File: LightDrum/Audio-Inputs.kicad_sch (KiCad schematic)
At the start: 52 parts, among them J201 XLR3, J202 SJ-43515RS-SMT-TR, Q201 NX6008NBKWX, Q202 NX6008NBKWX, U201 MCP3561R, U202 AZV321, U203 MCP3561R, U204 AZV321, U205 AP311A, U206 OPA1652

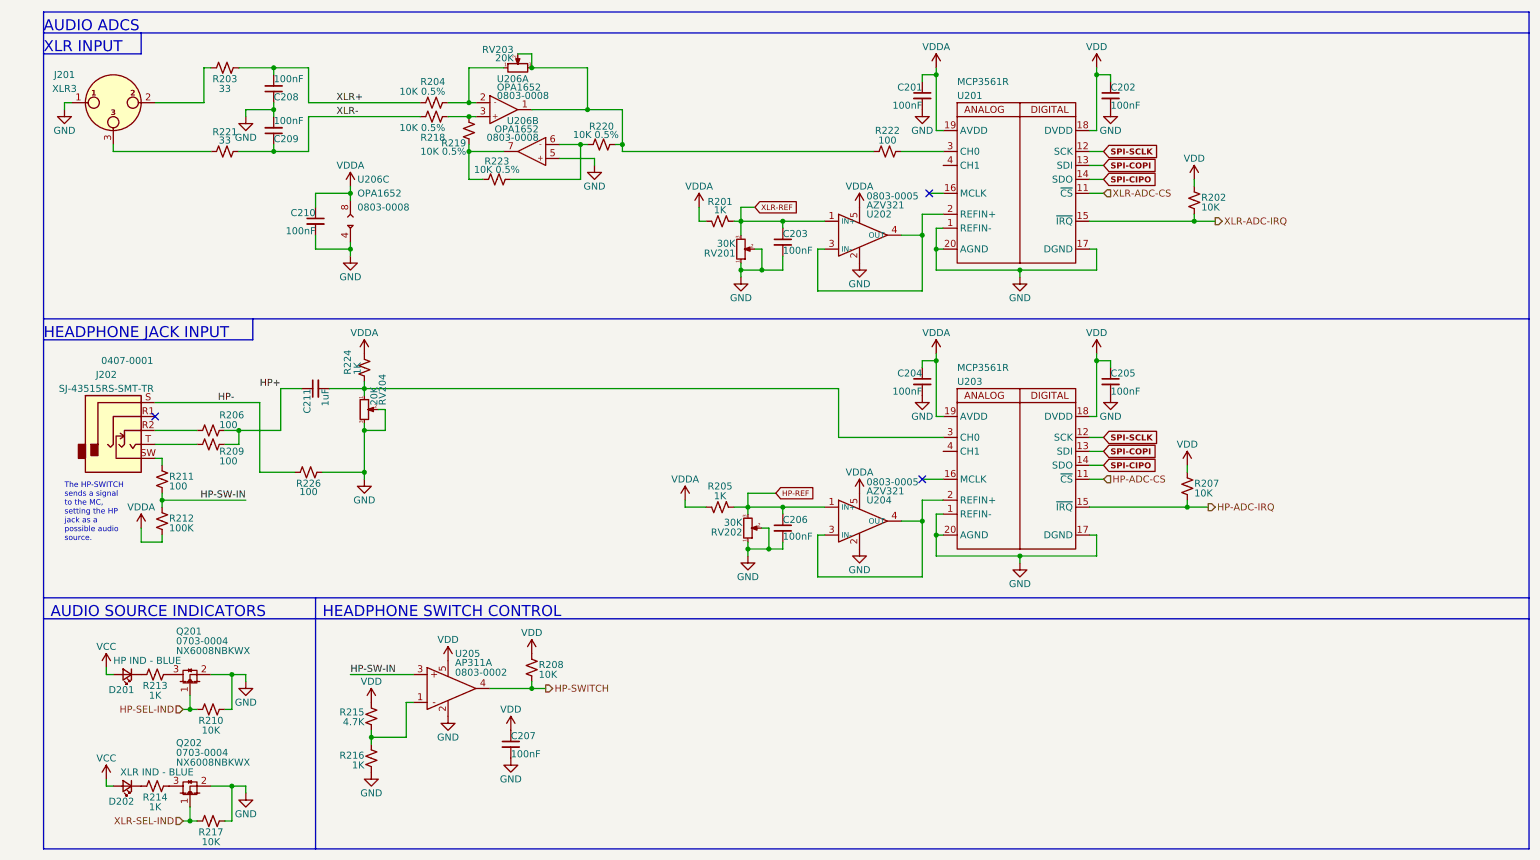
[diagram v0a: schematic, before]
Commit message: Preliminary schematic lock - Starting PCB layout
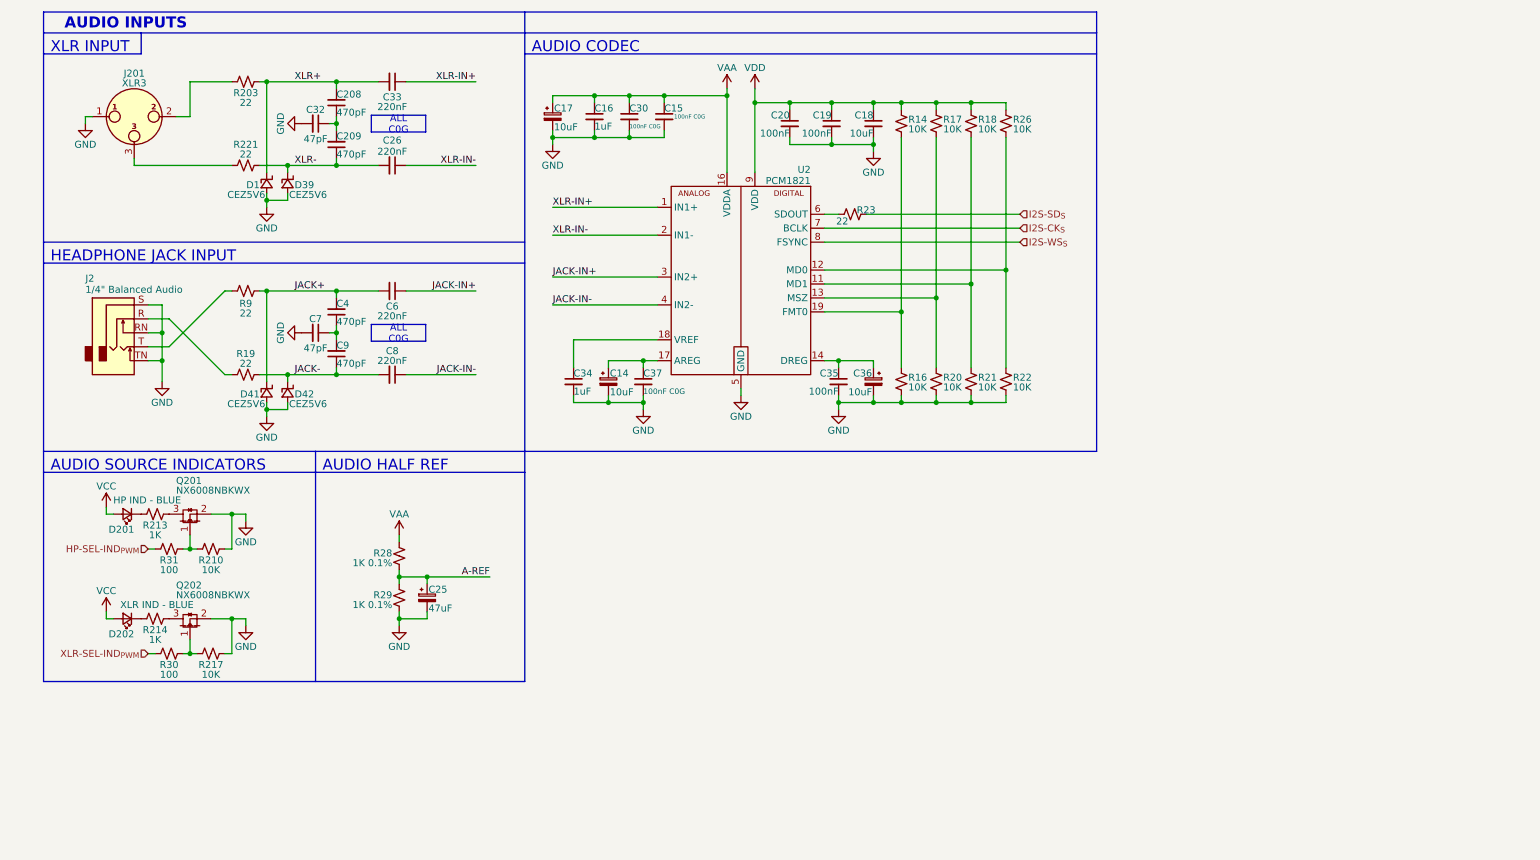
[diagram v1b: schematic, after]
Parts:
- removed C201, C202, C203, C204, C205, C206, C207, C210: 100nF, Capacitor_SMD:C_0603_1608Metric, symbol Device:C_Small
- removed C211: 1uF, Capacitor_SMD:C_0805_2012Metric, symbol Device:C_Small
- removed J201: XLR3, Daxxn_Connectors:CP30082-XLR, symbol Connector:XLR3
- removed J202: SJ-43515RS-SMT-TR, Daxxn_Connectors:SJ-43515RS-SMT-TR, symbol Daxxn_Connectors:SJ-43515RS-SMT-TR
- removed R201, R205: 1K, Resistor_SMD:R_0603_1608Metric, symbol Device:R_Small_US
- removed R202, R207: 10K, Resistor_SMD:R_0603_1608Metric, symbol Device:R_Small_US
- removed R204, R218, R219, R220, R223: 10K 0.5%, Resistor_SMD:R_0603_1608Metric, symbol Device:R_Small_US
- removed R206, R209, R211, R222: 100, Resistor_SMD:R_0805_2012Metric, symbol Device:R_Small_US
- removed R208: 10K, Resistor_SMD:R_0805_2012Metric, symbol Device:R_Small_US
- removed R212: 100K, Resistor_SMD:R_0805_2012Metric, symbol Device:R_Small_US
- removed R215: 4.7K, Resistor_SMD:R_0805_2012Metric, symbol Device:R_Small_US
- removed R216, R224: 1K, Resistor_SMD:R_0805_2012Metric, symbol Device:R_Small_US
- removed R226: 100, Resistor_SMD:R_0603_1608Metric, symbol Device:R_Small_US
- removed RV201, RV202: 30K, Daxxn_Switches:Bourns_3214W_Vertical, symbol Device:R_Potentiometer_Small
- removed RV203, RV204: 20K, Daxxn_Switches:Bourns_3214W_Vertical, symbol Device:R_Potentiometer_Small
- removed U201, U203: MCP3561R, Daxxn_Packages:QFN-20-1EP_3x3mm_P0.4mm_EP1.65x1.65mm, symbol Daxxn_IC:MCP3561R
- removed U202, U204: AZV321, Package_TO_SOT_SMD:SOT-23-5, symbol Daxxn_OPAMP:AZV321
- removed U205: AP311A, Package_TO_SOT_SMD:SOT-23-5, symbol Daxxn_OPAMP:AP311A
- removed U206: OPA1652, Package_SO:VSSOP-8_3.0x3.0mm_P0.65mm, symbol Daxxn_OPAMP:OPA1652
- added C14, C17, C36: 10uF, Capacitor_SMD:CP_Elec_3x5.4, symbol Daxxn_Device:C_Pol
- added C15, C30, C37: 100nF C0G, Capacitor_SMD:C_1206_3216Metric, symbol Device:C_Small
- added C16, C34: 1uF, Capacitor_SMD:C_0603_1608Metric, symbol Device:C_Small
- added C18: 10uF, Capacitor_SMD:C_1210_3225Metric, symbol Device:C_Small
- added C19, C20, C35: 100nF, Capacitor_SMD:C_0402_1005Metric, symbol Device:C_Small
- added C25: 47uF, Capacitor_SMD:CP_Elec_6.3x7.7, symbol Daxxn_Device:C_Pol
- added C26, C33, C6, C8: 220nF, Capacitor_SMD:C_1206_3216Metric, symbol Device:C_Small
- added C32, C7: 47pF, Capacitor_SMD:C_0402_1005Metric, symbol Device:C_Small
- added C4, C9: 470pF, Capacitor_SMD:C_0402_1005Metric, symbol Device:C_Small
- added D1, D39, D41, D42: CEZ5V6, Daxxn_Diodes:D_SOD-523, symbol Daxxn_Device:D_TVS_U
- added J2: 1/4" Balanced Audio, Daxxn_Connectors:SJ-63073E, symbol Daxxn_Connectors:AudioJack3_SwitchTR
- added J201: XLR3, Daxxn_Connectors:CP30082-XLR, symbol Connector_Audio:XLR3
- added R14, R16, R17, R18, R20, R21, R22, R26: 10K, Resistor_SMD:R_0402_1005Metric, symbol Device:R_Small_US
- added R19, R23, R9: 22, Resistor_SMD:R_0402_1005Metric, symbol Device:R_Small_US
- added R28, R29: 1K 0.1%, Resistor_SMD:R_0402_1005Metric, symbol Device:R_Small_US
- added R30, R31: 100, Resistor_SMD:R_0402_1005Metric, symbol Device:R_Small_US
- added U2: PCM1821, Daxxn_Packages:TI-WQFN-RTE-20-3x3mm-P0.5mm-EP1_1.4mm, symbol Daxxn_Audio:PCM1821
- C208, C209: value 100nF -> 470pF; footprint Capacitor_SMD:C_0603_1608Metric -> Capacitor_SMD:C_0402_1005Metric; SupplierPN (none) -> 1276-1117-1-ND
- D202: SupplierPN (none) -> LTST-S321TBKT
- Q201, Q202: SupplierPN (none) -> 1727-NX6008NBKWXCT-ND
- R203, R221: value 33 -> 22; footprint Resistor_SMD:R_0603_1608Metric -> Resistor_SMD:R_0402_1005Metric; SupplierPN (none) -> 2037-PFR05S-220-FNHCT-ND
- R210, R217: footprint Resistor_SMD:R_0805_2012Metric -> Resistor_SMD:R_0402_1005Metric; SupplierPN (none) -> 311-10KJRCT-ND
- R213, R214: footprint Resistor_SMD:R_0805_2012Metric -> Resistor_SMD:R_0402_1005Metric; SupplierPN (none) -> 311-1.0KJRCT-ND
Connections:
- net VDD: now also C18.1, C19.1, C20.1, R14.1, R17.1, R18.1, R26.1, U2.9 (VDD)
- net XLR+: now also C33.2, D1.1 (K)
- net XLR-: now also C26.2, D39.1 (K)
- net at R221.1: now also J201.3
- net at R203.1: now also J201.2
- net AGND renamed GND
- net GND: now also C14.2, C15.2, C16.2, C17.2, C18.2, C19.2, C20.2, C25.2, C30.2, C32.2, C34.2, C35.2, C36.2, C37.2, C7.2, D1.2 (A), D39.2 (A), D41.2 (A), D42.2 (A), J2.RN, J2.S, J2.TN, J201.1, R16.2, R20.2, R21.2, R22.2, R29.1, U2.10 (GND), U2.15 (GND), U2.20 (GND), U2.21 (GND), U2.5 (GND); no longer C208.1, C209.2
- net HP-SEL-IND: no longer names the net of Q201.1 (G), R210.2
- net HP-SEL-IND: now also R31.1
- net XLR-SEL-IND: no longer names the net of Q202.1 (G), R217.2
- net XLR-SEL-IND: now also R30.1
- new net: R17.2, R20.1, U2.13 (MSZ)
- new net: R18.2, R21.1, U2.11 (MD1)
- new net: R22.1, R26.2, U2.12 (MD0)
- new net: C35.1, C36.1, U2.14 (DREG)
- new net: C14.1, C37.1, U2.17 (AREG)
- new net: C34.1, U2.18 (VREF)
- new net: R14.2, R16.1, U2.19 (FMT0)
- new net: R23.2, U2.6 (SDOUT)
- new net: C4.1, C7.1, C9.2
- new net: J2.R, R19.1
- new net: J2.T, R9.1
- new net: C208.1, C209.2, C32.1
- new net A-REF: C25.1, R28.1, R29.2
- new net HP-SEL-IND_{PWM}: R31.2
- new net I2S-CK_{S}: U2.7 (BCLK)
- new net I2S-SD_{S}: R23.1
- new net I2S-WS_{S}: U2.8 (FSYNC)
- new net JACK+: C4.2, C6.2, D41.1 (K), R9.2
- new net JACK-: C8.2, C9.1, D42.1 (K), R19.2
- new net JACK-IN+: C6.1, U2.3 (IN2+)
- new net JACK-IN-: C8.1, U2.4 (IN2-)
- new net VAA: C15.1, C16.1, C17.1, C30.1, R28.2, U2.16 (VDDA)
- new net XLR-IN+: C33.1, U2.1 (IN1+)
- new net XLR-IN-: C26.1, U2.2 (IN1-)
- new net XLR-SEL-IND_{PWM}: R30.2
- no-connect marks 3 -> 0
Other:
- note added: "AUDIO CODEC"
- note added: "AUDIO HALF REF"
- note added: "AUDIO INPUTS"
- note removed: "AUDIO ADCS"
- note removed: "HEADPHONE SWITCH CONTROL"
- note removed: "The HP-SWITCH sends a signal to the MC, setting the HP jack as a possible audio source."
- moved on the sheet: C208, C209, D201, D202, Q201, Q202, R203, R210, R213, R214, R217, R221

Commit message: Component placement complete
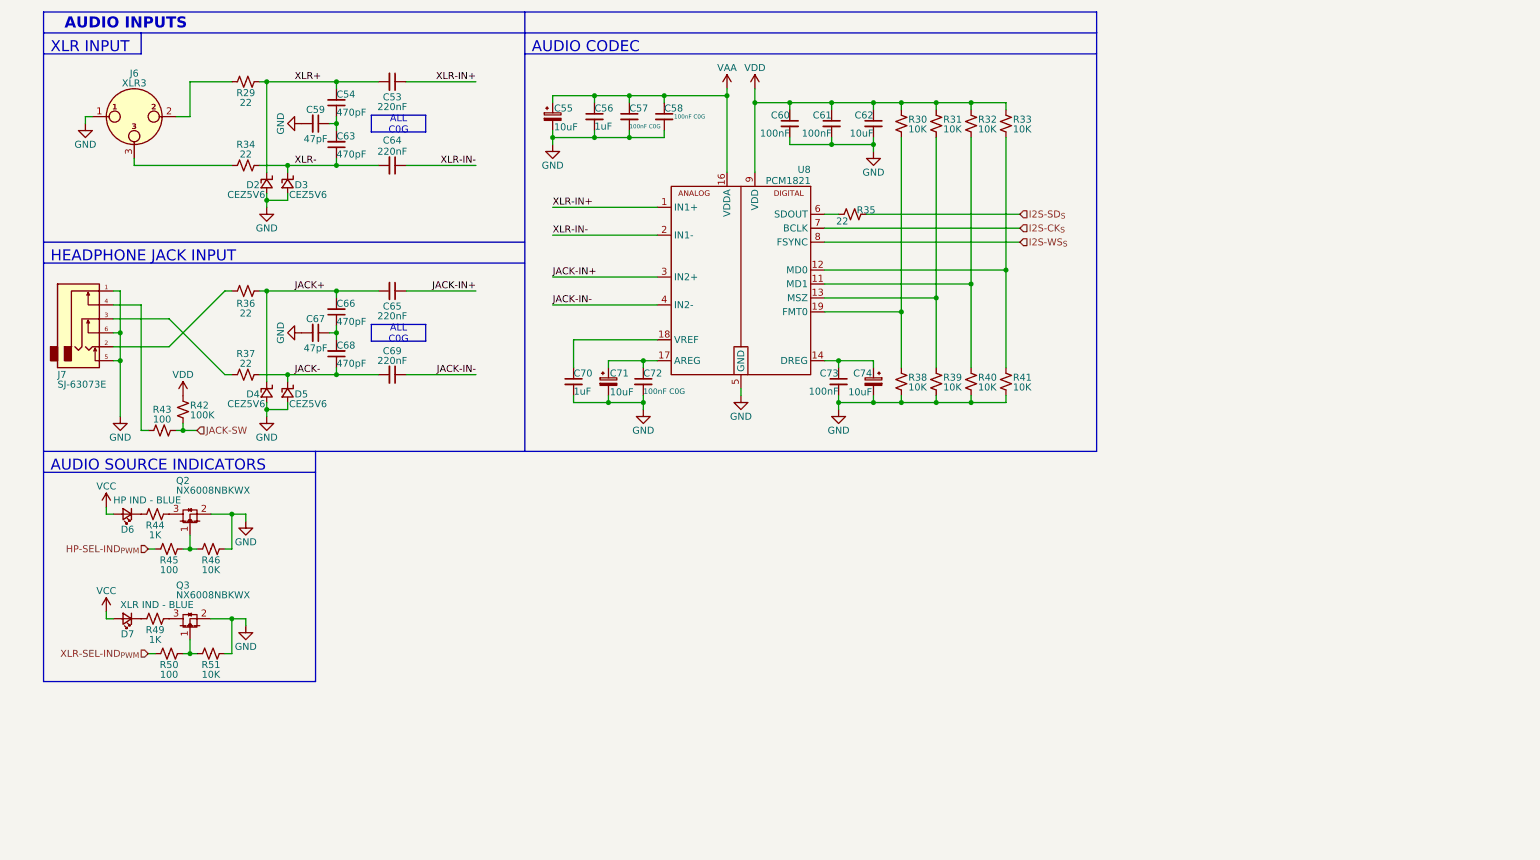
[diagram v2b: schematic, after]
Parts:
- removed C25: 47uF, Capacitor_SMD:CP_Elec_6.3x7.7, symbol Daxxn_Device:C_Pol
- removed J2: 1/4" Balanced Audio, Daxxn_Connectors:SJ-63073E, symbol Daxxn_Connectors:AudioJack3_SwitchTR
- removed R28, R29: 1K 0.1%, Resistor_SMD:R_0402_1005Metric, symbol Device:R_Small_US
- added J7: SJ-63073E, Daxxn_Connectors:SJ-63073E, symbol Daxxn_Connectors:SJ-63073E
- added R42: 100K, Resistor_SMD:R_0402_1005Metric, symbol Device:R_Small_US
- added R43: 100, Resistor_SMD:R_0402_1005Metric, symbol Device:R_Small_US
- renumbered C33 to C53, C208 to C54, C17 to C55, C16 to C56, C30 to C57, C15 to C58, C32 to C59, C20 to C60, C19 to C61, C18 to C62, C209 to C63, C26 to C64, C6 to C65, C4 to C66, C7 to C67, C9 to C68, C8 to C69, C34 to C70, C14 to C71, C37 to C72, C35 to C73, C36 to C74, D1 to D2, D39 to D3, D41 to D4, D42 to D5, D201 to D6, D202 to D7, J201 to J6, Q201 to Q2, Q202 to Q3, R203 to R29, R14 to R30, R17 to R31, R18 to R32, R26 to R33, R221 to R34, R23 to R35, R9 to R36, R19 to R37, R16 to R38, R20 to R39, R21 to R40, R22 to R41, R213 to R44, R31 to R45, R210 to R46, R214 to R49, R30 to R50, R217 to R51, U2 to U8
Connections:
- net GND: now also J7.1 (S), J7.5 (TN), J7.6 (RN)
- net VDD: now also R42.1
- net at R37.1: now also J7.3 (R)
- net at R36.1: now also J7.2 (T)
- new net: J7.4 (SN), R43.1
- new net JACK-SW: R42.2, R43.2
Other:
- note removed: "AUDIO HALF REF"

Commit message: Continuing layout
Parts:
- U8: footprint Daxxn_Packages:TI-WQFN-RTE-20-3x3mm-P0.5mm-EP1_1.4mm -> Daxxn_Packages:TI-WQFN-RTE_(CUSTOM)-20-3x3mm-P0.5mm-EP1_1.4mm
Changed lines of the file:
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@@
       (effects (font (size 1.27 1.27)) (justify left))
     )
-    (property "Footprint" "Daxxn_Packages:TI-WQFN-RTE-20-3x3mm-P0.5mm-EP1_1.4mm" (at 140.97 31.75 0)
+    (property "Footprint" "Daxxn_Packages:TI-WQFN-RTE_(CUSTOM)-20-3x3mm-P0.5mm-EP1_1.4mm" (at 140.97 31.75 0)
       (effects (font (size 1.27 1.27)) hide)
     )
@@
       (effects (font (size 1.27 1.27)) hide)
     )
+    (property "Schematic" "" (at 153.67 45.72 0)
+      (effects (font (size 1.27 1.27)) hide)
+    )
+    (property "PartNumber" "" (at 153.67 45.72 0)
+      (effects (font (size 1.27 1.27)))
+    )
     (pin "1")

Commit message: Minor fixes and cleanup - REV11
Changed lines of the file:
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@@
     (stroke (width 0) (type default))
   )
-  (polyline (pts (xy 63.5 97.79) (xy 63.5 135.89))
+  (polyline (pts (xy 57.15 97.79) (xy 57.15 135.89))
     (stroke (width 0) (type solid))
   )
@@
     (stroke (width 0) (type default))
   )
-  (polyline (pts (xy 63.5 135.89) (xy 13.97 135.89))
+  (polyline (pts (xy 57.15 135.89) (xy 13.97 135.89))
     (stroke (width 0) (type solid))
   )
@@
     (stroke (width 0) (type default))
   )
-  (polyline (pts (xy 13.97 97.79) (xy 63.5 97.79))
+  (polyline (pts (xy 13.97 97.79) (xy 57.15 97.79))
     (stroke (width 0) (type solid))
   )
@@
     (stroke (width 0) (type default))
   )
-  (polyline (pts (xy 63.5 93.98) (xy 101.6 93.98))
+  (polyline (pts (xy 57.15 93.98) (xy 101.6 93.98))
     (stroke (width 0) (type default))
   )
@@
     (stroke (width 0) (type solid))
   )
-  (polyline (pts (xy 13.97 93.98) (xy 63.5 93.98))
+  (polyline (pts (xy 13.97 93.98) (xy 57.15 93.98))
     (stroke (width 0) (type solid))
   )
@@
     (stroke (width 0) (type default))
   )
-  (polyline (pts (xy 63.5 93.98) (xy 63.5 97.79))
-    (stroke (width 0) (type solid))
-  )
+  (polyline (pts (xy 57.15 93.98) (xy 57.15 97.79))
+    (stroke (width 0) (type solid))
+  )

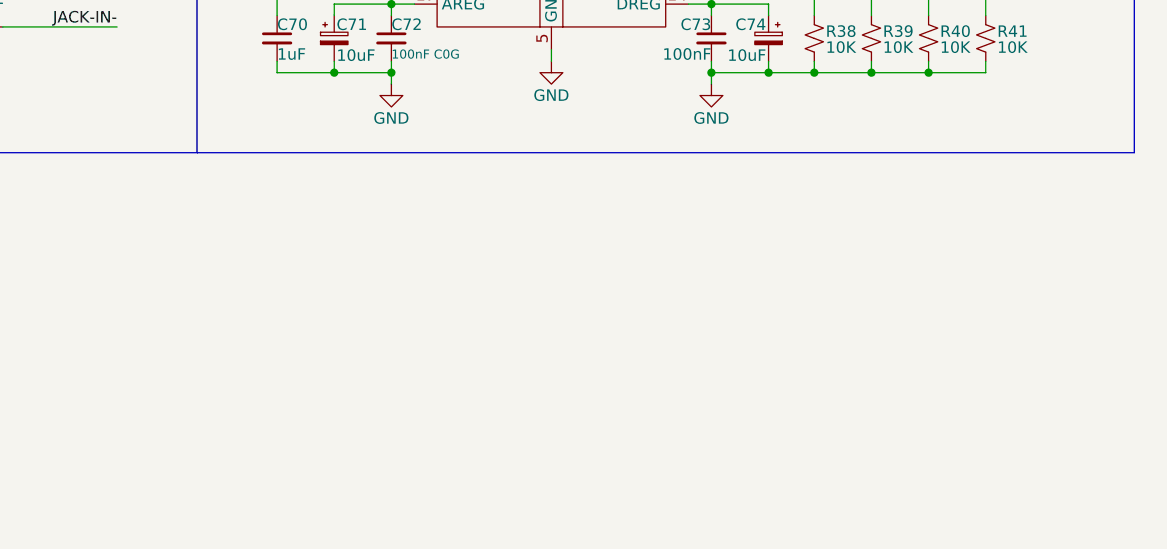
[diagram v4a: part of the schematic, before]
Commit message: Fix backwards Connector - Initial Testing
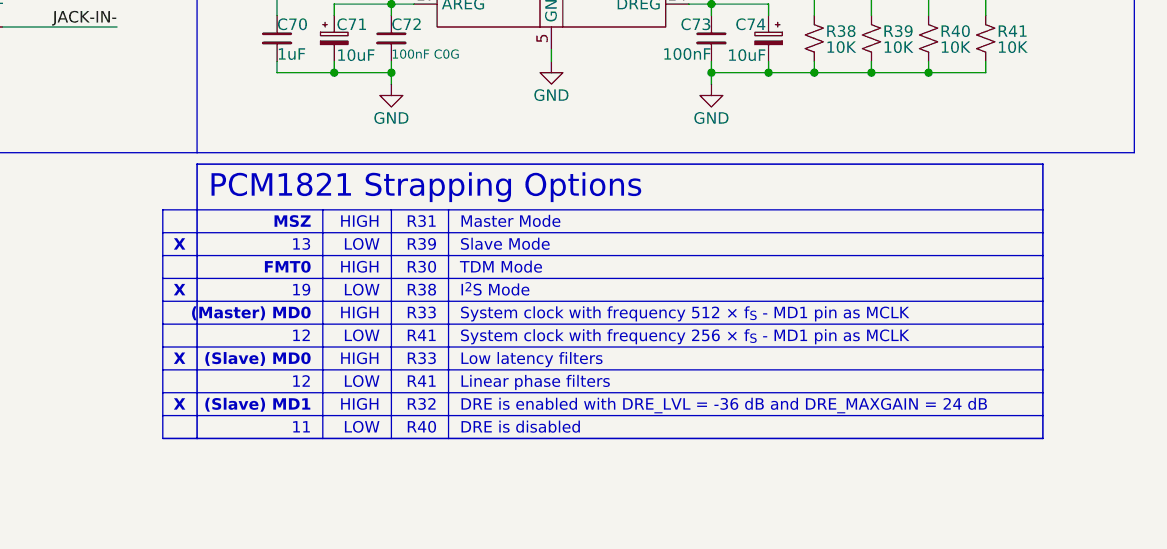
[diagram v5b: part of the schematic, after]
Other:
- note added: "(Master) MD0"
- note added: "(Slave) MD0"
- note added: "(Slave) MD1"
- note added: "11"
- note added: "12"
- note added: "13"
- note added: "19"
- note added: "DRE is disabled"
- note added: "DRE is enabled with DRE_LVL = -36 dB and DRE_MAXGAIN = 24 dB"
- note added: "FMT0"
- note added: "HIGH"
- note added: "I^{2}S Mode"
- note added: "LOW"
- note added: "Linear phase filters"
- note added: "Low latency filters"
- note added: "MSZ"
- note added: "Master Mode"
- note added: "PCM1821 Strapping Options"
- note added: "R30"
- note added: "R31"
- note added: "R32"
- note added: "R33"
- note added: "R38"
- note added: "R39"
- note added: "R40"
- note added: "R41"
- note added: "Slave Mode"
- note added: "System clock with frequency 256 × f_{S} - MD1 pin as MCLK"
- note added: "System clock with frequency 512 × f_{S} - MD1 pin as MCLK"
- note added: "TDM Mode"
- note added: "X"

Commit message: Replace DSub with much better ECU conn
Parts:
- removed D6: HP IND - BLUE, Daxxn_LEDs:LTST-S321TBKT, symbol Device:LED_Small
- removed D7: XLR IND - BLUE, Daxxn_LEDs:LTST-S321TBKT, symbol Device:LED_Small
- added D6: HP IND - BLUE, Daxxn_LEDs:LTST-S321TBKT, symbol Daxxn_Device:LED-K
- added D7: XLR IND - BLUE, Daxxn_LEDs:LTST-S321TBKT, symbol Daxxn_Device:LED-K
- U8: PartNumber (none) -> 0823-00002
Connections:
- net VCC: now also D6.1 (K), D7.1 (K)
- net at R49.2: now also D7.2 (A)
- net at R44.2: now also D6.2 (A)

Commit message: Organize old files and generate interface gerbers
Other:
- moved on the sheet: D7, Q3, R49, R50, R51

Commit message: (WIP) REV12 Testing and firmware dev
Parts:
- removed R35: 22, Resistor_SMD:R_0402_1005Metric, symbol Device:R_Small_US
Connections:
- net I2S-SD_{S}: now also U8.6 (SDOUT)
